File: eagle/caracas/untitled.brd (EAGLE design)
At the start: 65 x 56.5 mm, 20 parts, among them IC1 4011N, Q1 IRLZ44Z, X1 22-23-2021, X2 22-23-2021, X3 22-23-2021, X5 22-23-2021, X6 22-23-2091

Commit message: Update schematics again
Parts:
- added C1: (no value), rcl:E2,5-6E
- added R6: 260, rcl:0207/10
- added R7: 115, rcl:0207/10
- added T3: (no value), transistor:TO92-CBE
- moved R5 8.27 mm to (15.2, 32.3)
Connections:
- new net N$18: R6.2, T3.B
- new net N$19: R6.1, RASPBERRYPI.32
- new net POWER_CONTROL: R7.2, T3.E, U$1.P$2
- net +5V: now also C1.+; no longer U$1.P$2
- net +5V_SW_GND: now also C1.-
- net GND: now also R7.1
- net VCC: now also T3.C
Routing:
- net POWER_CONTROL: track 0.00 -> 86.3 mm
- net VCC: track 74.8 -> 132.0 mm
- net N$19: track 0.00 -> 34.9 mm
- net N$15: track 13.4 -> 25.1 mm
- net N$16: track 16.1 -> 27.5 mm
- net GND: track 0.00 -> 9.94 mm
- net N$18: track 0.00 -> 9.16 mm
- net N$9: track 17.5 -> 10.9 mm
- net N$11: track 40.0 -> 44.0 mm
- net N$2: track 31.3 -> 35.0 mm
- net N$1: track 109.2 -> 112.7 mm
- net +5V: track 64.8 -> 61.3 mm
- net POWER_STATE: track 64.0 -> 66.2 mm
- net MOSFET_ON: track 8.67 -> 7.36 mm
- net +3.3V: track 49.3 -> 50.5 mm

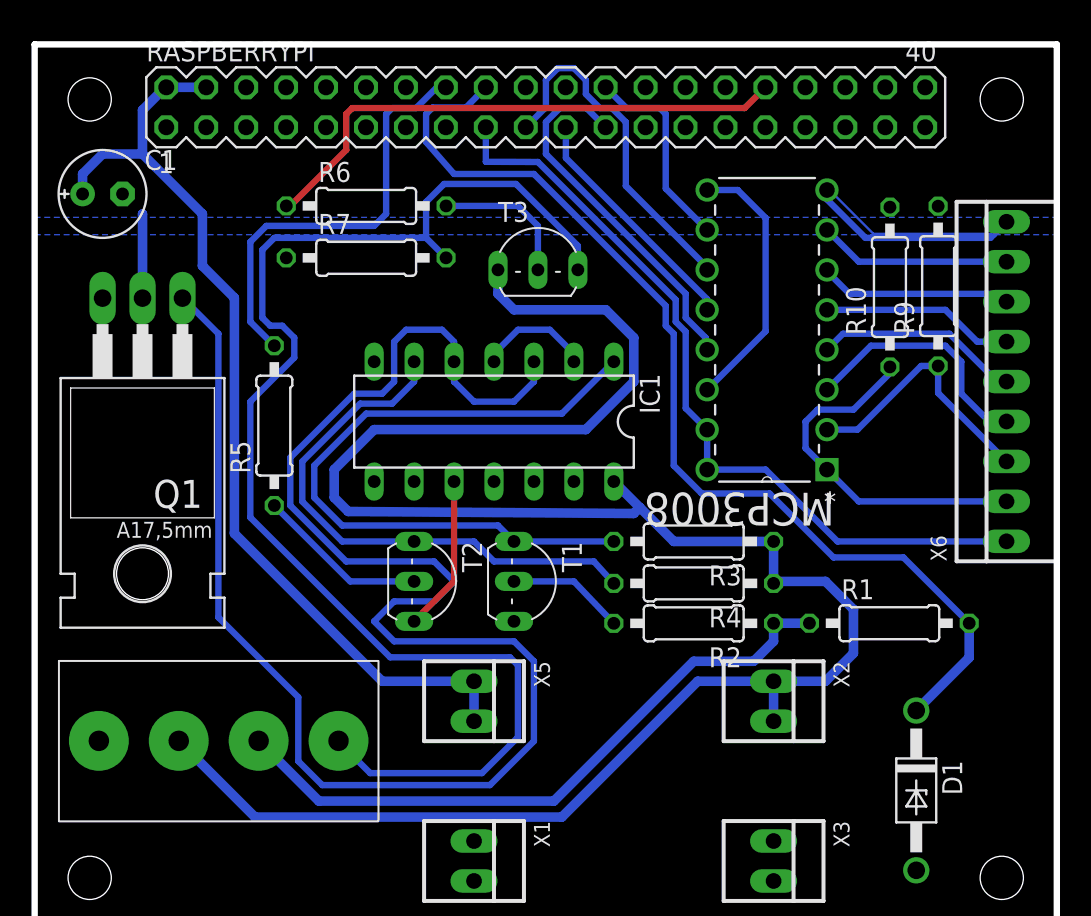
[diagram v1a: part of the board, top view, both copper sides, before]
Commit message: Power board: route power buses on top layer
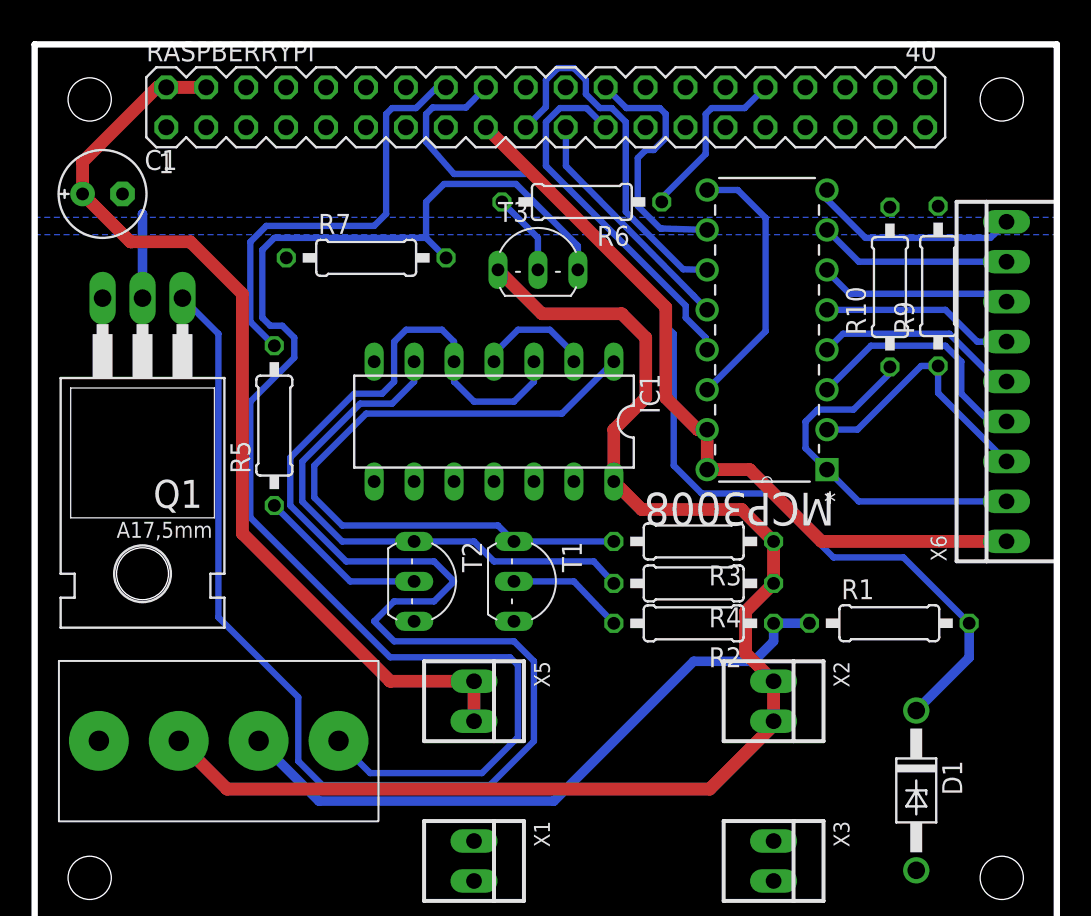
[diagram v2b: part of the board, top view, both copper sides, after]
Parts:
- moved R6 13.7 mm to (34.8, 46.5), turned to 180 degrees
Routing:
- net VCC: track 132.0 -> 86.8 mm
- net N$19: track 34.9 -> 11.2 mm
- net N$15: track 25.1 -> 13.5 mm
- net GND: track 9.94 -> 0.00 mm
- net N$18: track 9.16 -> 5.26 mm
- net N$13: track 13.0 -> 16.4 mm
- net +3.3V: track 50.5 -> 48.9 mm
- net N$5: track 22.4 -> 23.3 mm

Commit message: Final board v2.0
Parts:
- C1: value (none) -> 0.1µ
- moved T3 0.76 mm to (32.0, 41.4)
- renumbered IC1 to 4011, RASPBERRYPI to RASPBERRY_PI_GPIO, X1 to GND_1, X2 to 12V_IN, X3 to GND_2, X5 to +5VOUT, X6 to ADC
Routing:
- net POWER_CONTROL: track 86.3 -> 87.0 mm
- net N$18: track 5.26 -> 6.03 mm
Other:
- outline, holes or cut-outs redrawn
- board text added: "+12V"
- board text added: "+12V IGN"
- board text added: "+3.3V"
- board text added: "+5V"
- board text added: "1"
- board text added: "2"
- board text added: "3"
- board text added: "4"
- board text added: "5"
- board text added: "6"
- board text added: "7"
- board text added: "8"
- board text added: "Caracas Power board v2.0"
- board text added: "GND"
- board text added: "PWR CTRL"

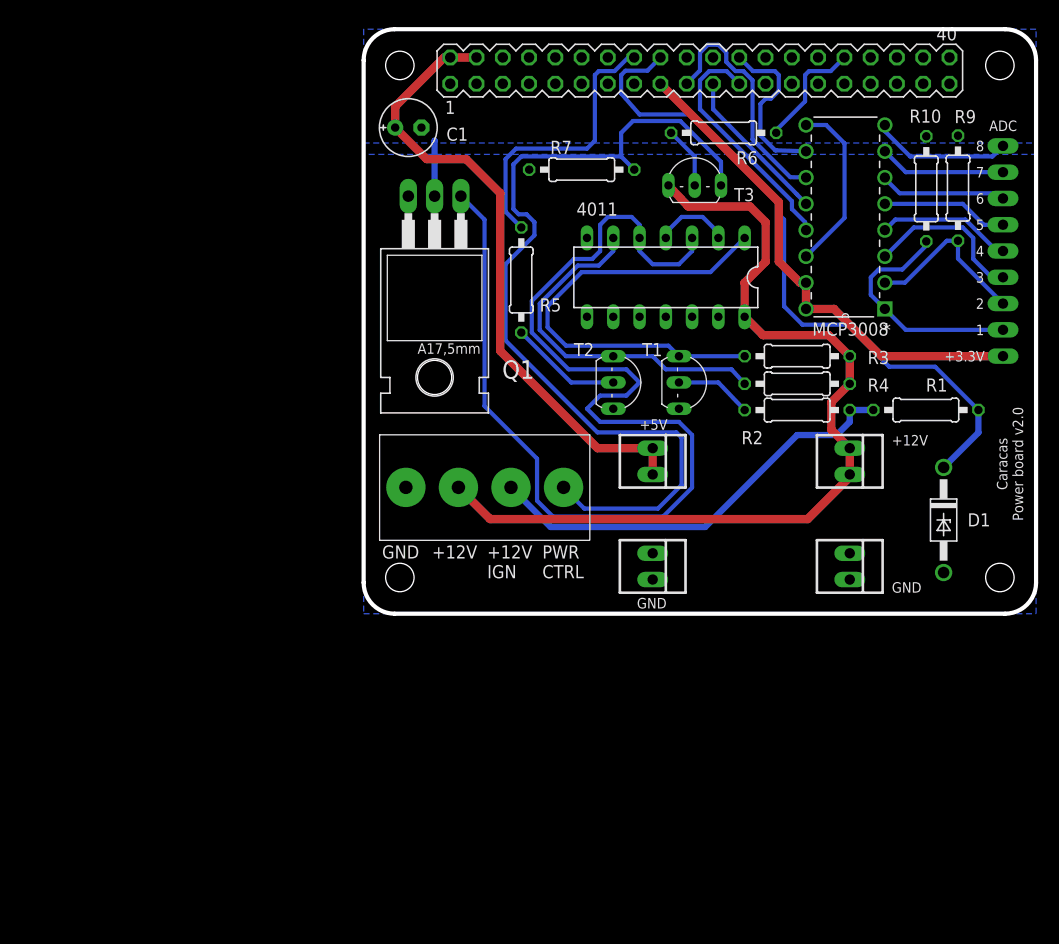
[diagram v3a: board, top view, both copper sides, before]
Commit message: Power board v2 does not work, start working on v3
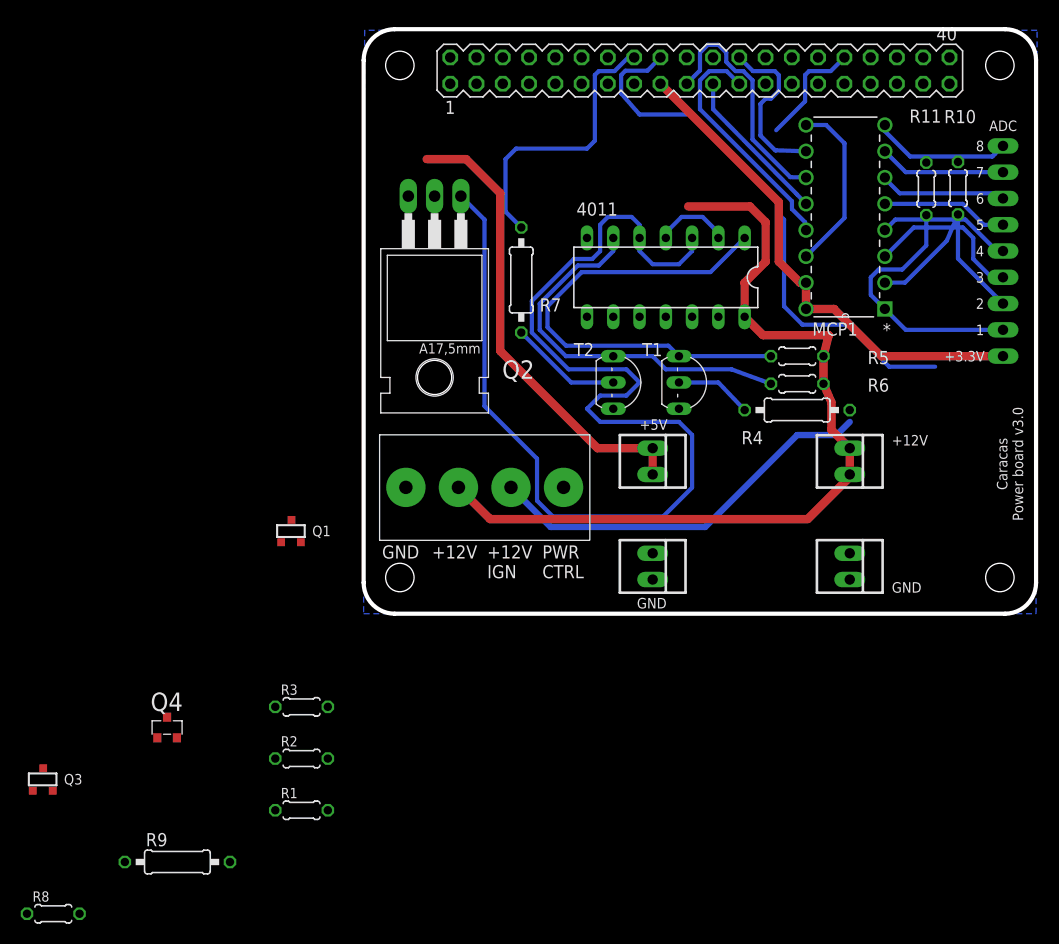
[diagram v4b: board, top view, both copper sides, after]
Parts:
- removed C1: 0.1µ, rcl:E2,5-6E
- removed D1: 1N4728, diode:DO41Z10
- removed T3: (no value), transistor:TO92-CBE
- added Q2: IRF9530, transistor-fet:TO220
- added Q3: (no value), transistors:SOT-23
- added Q4: IRLML5203, transistor-power:MICRO3
- added R11: 1k, rcl:0204/5
- added R8: 10k, rcl:0204/5
- Q1: value IRLZ44Z -> (none); device transistor-power:TO220BH -> transistors:SOT-23
- R1: value 870 -> 10k; device rcl:0207/10 -> rcl:0204/5
- R10, R3: device rcl:0207/10 -> rcl:0204/5
- R2: value 1.2k -> 10k; device rcl:0207/10 -> rcl:0204/5
- R4: value 10k -> 1.2k
- R5, R6: value 260 -> 10k; device rcl:0207/10 -> rcl:0204/5
- R7: value 115 -> 260
- moved R9 99.7 mm to (-18.0, -24.0), turned to 0 degrees
- moved R1 71.7 mm to (-6.00, -19.0)
- moved R3 58.7 mm to (-6.00, -9.00), turned to 0 degrees
- moved R2 58.6 mm to (-6.00, -14.0), turned to 0 degrees
- moved Q1 29.5 mm to (-7.00, 8.00), turned to 0 degrees
- moved R5 27.7 mm to (41.9, 24.9), turned to 180 degrees
- moved R6 25.3 mm to (41.9, 22.2)
- moved R7 12.2 mm to (15.2, 32.3), turned to 90 degrees
- moved R10 3.06 mm to (57.5, 41.1)
- moved R4 2.54 mm to (41.9, 19.7)
- renumbered MCP3008 to MCP1, U$1 to EXT
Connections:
- removed net +5V_SW_GND: C1.-, MCP1.14, MCP1.9, Q1.D, R10.2, R9.2, RASPBERRY_PI_GPIO.6
- removed net POWER_CONTROL: EXT.P$2, R7.2, T3.E
- new net N$17: Q2.2, RASPBERRY_PI_GPIO.2, RASPBERRY_PI_GPIO.4
- new net N$21: Q1.3, R1.2
- new net N$22: Q3.3, Q4.1, R9.1
- new net PWR_CTRL: EXT.P$2, Q4.3
- net +12V_IGN: now also R2.2, R3.2, R4.1; no longer R1.1, R2.1
- net +5V: now also Q2.3; no longer C1.+, RASPBERRY_PI_GPIO.2, RASPBERRY_PI_GPIO.4
- net ANA_0: now also R11.1; no longer R10.1
- net ANA_1: now also R10.1; no longer R9.1
- net GND: now also MCP1.14, MCP1.9, Q1.2, Q3.2, R10.2, R11.2, R3.1, R8.1, RASPBERRY_PI_GPIO.6; no longer 4011.10, 4011.11, D1.A, Q1.S, R7.1
- net MOSFET_ON: now also Q2.1
- net N$1: no longer Q1.G
- net N$11: now also R5.2; no longer R3.2
- net N$12: now also R4.2; no longer R2.2
- net N$16: now also R7.2; no longer R5.2
- net N$18: now also Q1.1, R2.1; no longer R6.2, T3.B
- net N$19: now also Q3.1, R8.2; no longer R6.1
- net N$2: now also R6.2; no longer R4.2
- net N$9: now also R7.1; no longer R5.1
- net POWER_STATE: now also R1.1; no longer D1.C, R1.2
- net VCC: now also Q4.2, R5.1, R6.1, R9.2; no longer R3.1, R4.1, T3.C
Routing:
- net POWER_CONTROL: track 87.0 -> 0.00 mm
- net +5V_SW_GND: track 22.3 -> 0.00 mm
- net GND: track 0.00 -> 16.9 mm
- net +5V: track 61.1 -> 44.9 mm
- net POWER_STATE: track 66.2 -> 53.3 mm
- net N$18: track 6.03 -> 0.00 mm
- net ANA_1: track 16.6 -> 20.8 mm
- net VCC: track 86.6 -> 82.4 mm
- net +12V_IGN: track 42.0 -> 38.5 mm
- net N$11: track 44.0 -> 46.6 mm
- net ANA_0: track 22.9 -> 25.5 mm
- net N$2: track 35.0 -> 37.2 mm
- removed copper zone on layer 16, net +5V_SW_GND
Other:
- board text added: "Caracas Power board v3.0"
- board text removed: "Caracas Power board v2.0"

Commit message: More schematics WIP
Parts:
- removed Q4: IRLML5203, transistor-power:MICRO3
- removed T1, T2: (no value), transistor:TO92-CBE
- Q1: value (none) -> AO4842; device transistors:SOT-23 -> caracas:8-SOIC
- Q2: value IRF9530 -> AO4842; device transistor-fet:TO220 -> caracas:8-SOIC
- Q3: value (none) -> AO4807; device transistors:SOT-23 -> caracas:8-SOIC
- R1, R10, R11, R2, R3, R5, R6, R8: device rcl:0204/5 -> rcl:0207/10
- R4: value 1.2k -> 10k
- R7: value 260 -> 10k
- moved R8 88.2 mm to (21.0, 43.0)
- moved R9 80.1 mm to (21.0, 46.0)
- moved R1 59.9 mm to (9.00, 39.0)
- moved R2 58.7 mm to (8.00, 43.0)
- moved R3 57.0 mm to (9.00, 46.0)
- moved Q3 54.0 mm to (3.00, 26.0), turned to 270 degrees
- moved Q1 33.2 mm to (24.0, 20.0)
- moved R4 29.2 mm to (21.0, 40.0), turned to 0 degrees
- moved Q2 13.1 mm to (12.0, 22.0), turned to 0 degrees
- moved R7 7.46 mm to (21.0, 37.0), turned to 0 degrees
- moved R10 3.06 mm to (54.4, 41.1)
- moved R11 3.06 mm to (57.5, 41.1)
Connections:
- removed net N$16: R7.2, RASPBERRY_PI_GPIO.16
- removed net N$9: R7.1, T2.B
- new net SUICIDE_SIGNAL: Q1.P$2, R7.2, RASPBERRY_PI_GPIO.16
- net +5V: now also Q3.P$1; no longer Q2.3
- net ANA_0: now also R10.1; no longer R11.1
- net ANA_1: now also R11.1; no longer R10.1
- net GND: now also Q1.P$1, Q1.P$3, Q2.P$1, Q2.P$3, R7.1; no longer Q1.2, Q3.2, T1.E, T2.E
- net MOSFET_ON: now also Q3.P$2; no longer Q2.1
- net N$11: now also Q1.P$5, Q1.P$6; no longer T1.C
- net N$12: now also Q1.P$4; no longer T1.B
- net N$17: now also Q3.P$7, Q3.P$8; no longer Q2.2
- net N$18: now also Q2.P$2; no longer Q1.1
- net N$19: now also Q2.P$4; no longer Q3.1
- net N$2: now also Q1.P$7, Q1.P$8; no longer T2.C
- net N$21: now also Q2.P$7, Q2.P$8; no longer Q1.3
- net N$22: now also Q2.P$5, Q2.P$6, Q3.P$4; no longer Q3.3, Q4.1
- net PWR_CTRL: now also Q3.P$5, Q3.P$6; no longer Q4.3
- net VCC: now also Q3.P$3; no longer Q4.2
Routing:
- net N$1: track 112.7 -> 8.67 mm
- net N$11: track 46.6 -> 0.00 mm
- net +5V: track 44.9 -> 2.54 mm
- net N$2: track 37.2 -> 0.00 mm
- net N$16: track 27.5 -> 0.00 mm
- net N$9: track 10.9 -> 0.00 mm
- net N$12: track 7.49 -> 0.00 mm
- net SUICIDE_SIGNAL: track 0.00 -> 4.50 mm
- net ANA_1: track 20.8 -> 16.6 mm
- net ANA_0: track 25.5 -> 22.9 mm
- net +12V_IGN: track 38.5 -> 37.2 mm
- net VCC: track 82.4 -> 83.1 mm

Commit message: Complete rework of the PCB
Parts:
- removed MCP1: MCP3008-I/P, mpc3008:DIP254P762X432-16
- added MCP3008: MCP3008-I/P, mpc3008:DIP254P762X432-16
- added R12, R13, R14, R15, R16, R17: 1k, rcl:0207/10
- moved GND_2 45.8 mm to (5.57, 24.0), turned to 180 degrees
- moved R3 44.6 mm to (32.5, 8.08), turned to 270 degrees
- moved GND_1 44.5 mm to (5.57, 43.1), turned to 180 degrees
- moved R2 41.1 mm to (29.7, 8.08), turned to 270 degrees
- moved R9 38.4 mm to (26.9, 8.08), turned to 270 degrees
- moved R11 35.8 mm to (43.7, 8.13)
- moved R10 35.6 mm to (40.9, 8.13)
- moved R4 35.0 mm to (35.3, 8.08), turned to 90 degrees
- moved 12V_IN 32.6 mm to (15.7, 24.0), turned to 180 degrees
- moved +5VOUT 30.8 mm to (15.7, 43.1), turned to 180 degrees
- moved Q2 23.5 mm to (35.4, 20.6), turned to 180 degrees
- moved Q3 18.9 mm to (21.8, 25.4)
- moved R1 18.3 mm to (26.9, 42.7), turned to 270 degrees
- moved Q1 14.6 mm to (22.6, 34.5), turned to 270 degrees
- moved 4011 8.14 mm to (34.9, 38.4), turned to 270 degrees
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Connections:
- removed net GND: 4011.12, 4011.13, 4011.7, 4011.8, 4011.9, EXT.P$1, GND_1.1, GND_1.2, GND_2.1, GND_2.2, MCP1.14, MCP1.9, Q1.P$1, Q1.P$3, Q2.P$1, Q2.P$3, R10.2, R11.2, R3.1, R7.1, R8.1, RASPBERRY_PI_GPIO.6
- removed net N$19: Q2.P$4, R8.2, RASPBERRY_PI_GPIO.32
- new net GND@BOTTOM: 4011.12, 4011.13, 4011.7, 4011.8, 4011.9, EXT.P$1, GND_1.1, GND_1.2, GND_2.1, GND_2.2, MCP3008.14, MCP3008.9, Q1.P$1, Q1.P$3, Q2.P$1, Q2.P$3, R10.1, R11.1, R12.1, R13.1, R14.1, R15.1, R16.1, R17.1, R3.1, R7.1, R8.1, RASPBERRY_PI_GPIO.9
- new net POWER_CONTROL: Q2.P$4, R8.2, RASPBERRY_PI_GPIO.11
- net +12V_IGN: now also EXT.P$3; no longer EXT.P$4
- net +3.3V: now also MCP3008.15, MCP3008.16; no longer MCP1.15, MCP1.16
- net ANA_0: now also MCP3008.1, R10.2; no longer MCP1.1, R10.1
- net ANA_1: now also MCP3008.2, R11.2; no longer MCP1.2, R11.1
- net N$10: now also MCP3008.6, R15.2; no longer MCP1.6
- net N$13: now also MCP3008.10; no longer MCP1.10
- net N$14: now also MCP3008.7, R16.2; no longer MCP1.7
- net N$15: now also MCP3008.8, R17.2; no longer MCP1.8
- net N$3: now also MCP3008.13; no longer MCP1.13
- net N$4: now also MCP3008.12; no longer MCP1.12
- net N$5: now also MCP3008.11; no longer MCP1.11
- net N$6: now also MCP3008.3, R12.2; no longer MCP1.3
- net N$7: now also MCP3008.4, R13.2; no longer MCP1.4
- net N$8: now also MCP3008.5, R14.2; no longer MCP1.5
- net PWR_CTRL: now also EXT.P$4; no longer EXT.P$2
- net VCC: now also EXT.P$2; no longer EXT.P$3
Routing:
- net MOSFET_ON: track 7.36 -> 91.9 mm
- net N$17: track 0.00 -> 56.2 mm
- net POWER_STATE: track 53.3 -> 6.75 mm
- net POWER_CONTROL: track 0.00 -> 39.1 mm
- net N$21: track 0.00 -> 35.1 mm
- net N$22: track 0.00 -> 33.1 mm
- net N$14: track 12.3 -> 42.9 mm
- net N$10: track 12.3 -> 42.9 mm
- net N$8: track 12.3 -> 42.7 mm
- net N$11: track 0.00 -> 29.2 mm
- net N$7: track 13.1 -> 41.4 mm
- net N$15: track 13.5 -> 41.2 mm
- net VCC: track 83.1 -> 108.8 mm
- net N$6: track 15.8 -> 40.5 mm
- net N$12: track 0.00 -> 24.3 mm
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- added copper zone on layer 16, net GND@BOTTOM
- removed copper zone on layer 16, net GND
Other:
- board text added: "Caracas v3.0 kim@incendio.no"
- board text removed: "Caracas Power board v3.0"
